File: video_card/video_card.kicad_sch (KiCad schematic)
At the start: 22 parts, among them J1 Bus, J2 DE15_Receptacle_HighDensity, J3 H_SYNC_TEST, J4 V_SYNC_TEST, J5 VSYNC_INT_EN, J6 INT_EN, U1 Upduino v3.1, U2 25.175 MHz, U3 SN74LVC4245A, U4 SN74LVC4245A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

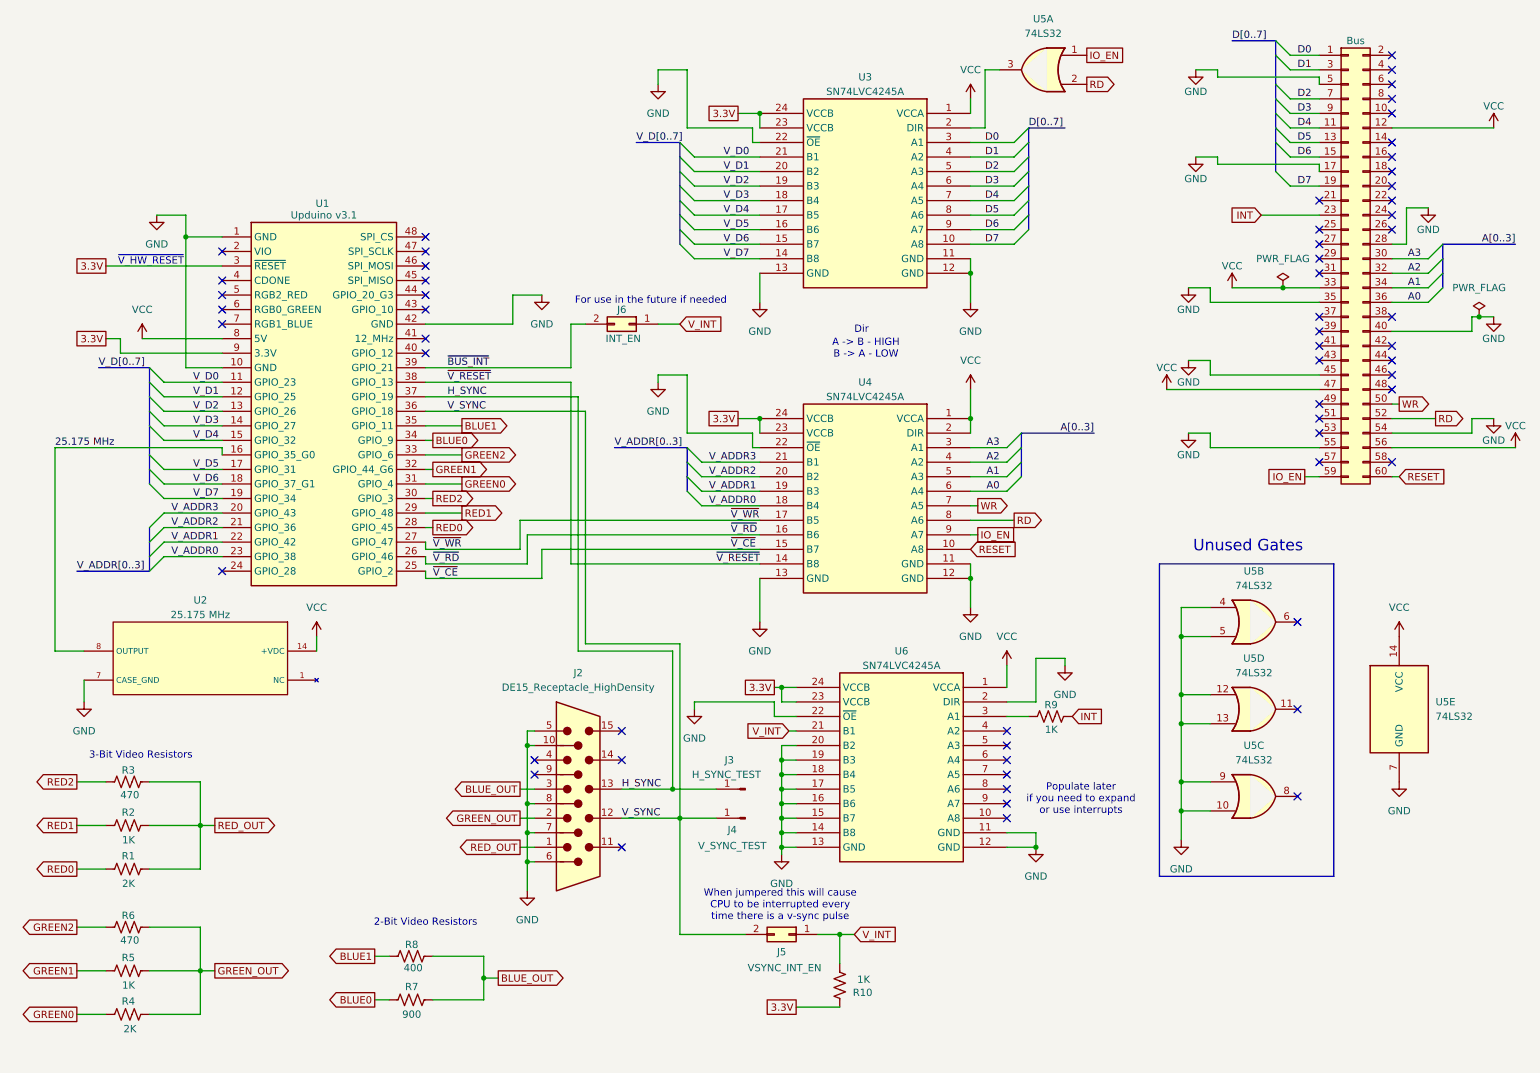
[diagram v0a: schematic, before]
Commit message: Swapped out '4245' on the INT signal to a more simple transistor circuit
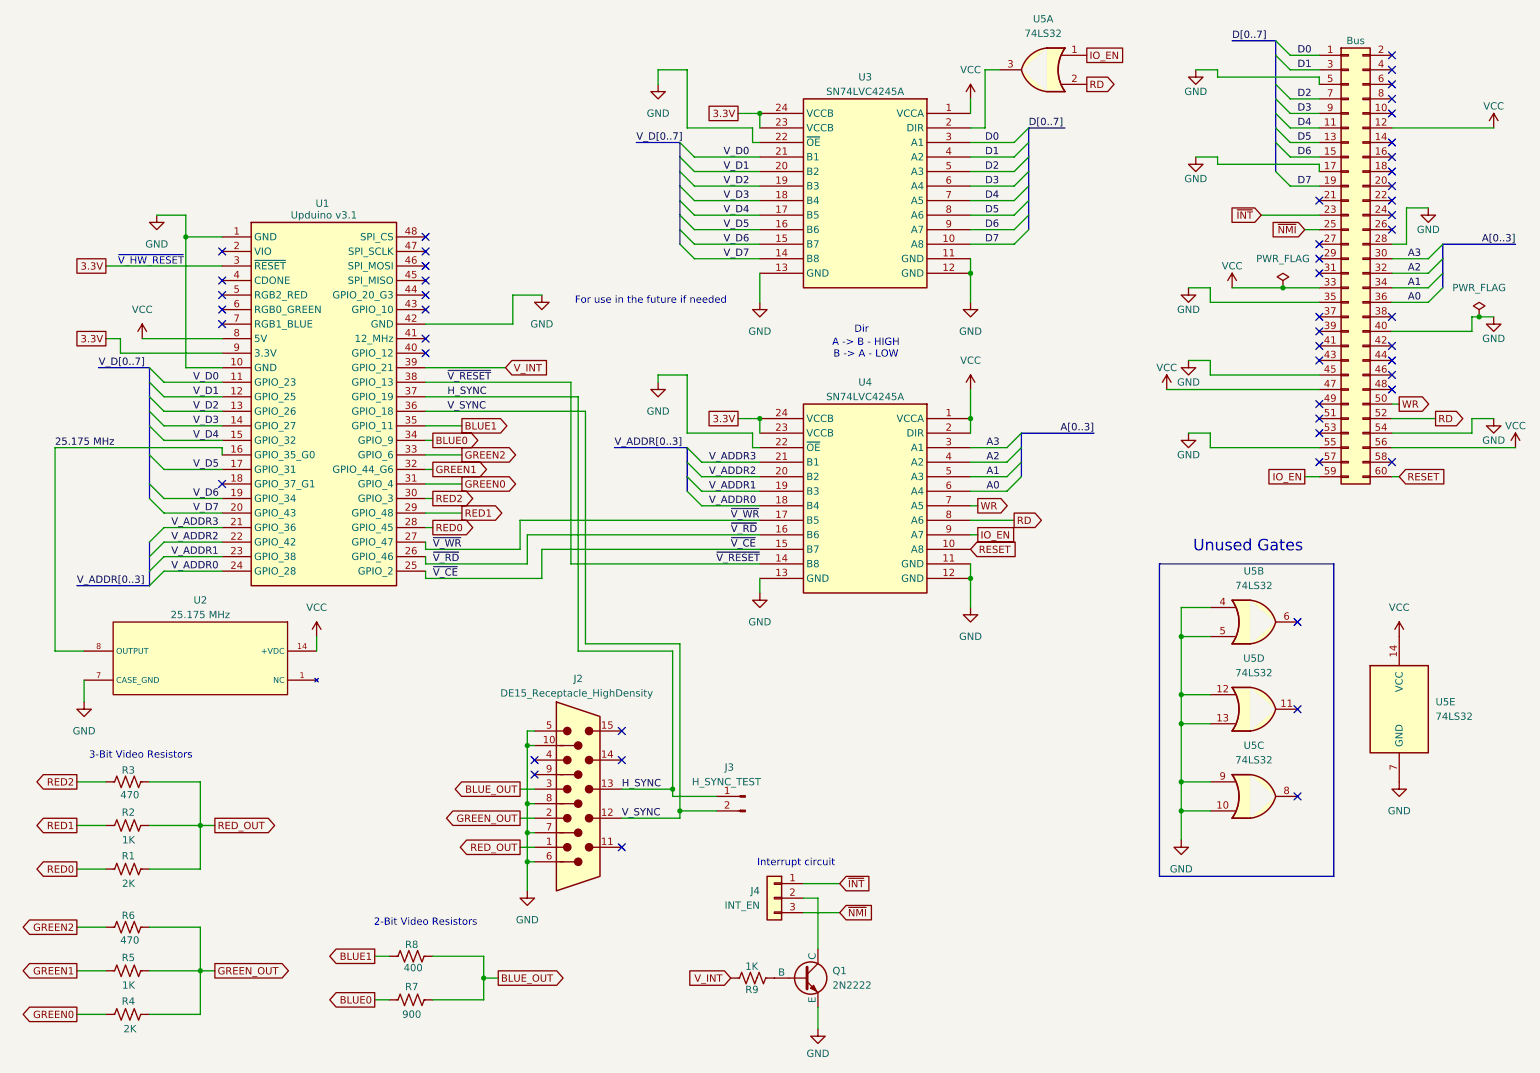
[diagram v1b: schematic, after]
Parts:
- removed J4: V_SYNC_TEST, Connector_PinHeader_2.54mm:PinHeader_1x01_P2.54mm_Vertical, symbol Connector:Conn_01x01_Pin
- removed J5: VSYNC_INT_EN, Connector_PinHeader_2.54mm:PinHeader_2x01_P2.54mm_Vertical, symbol Connector_Generic:Conn_02x01
- removed J6: INT_EN, Connector_PinHeader_2.54mm:PinHeader_2x01_P2.54mm_Vertical, symbol Connector_Generic:Conn_02x01
- removed R10: 1K, Resistor_THT:R_Axial_DIN0207_L6.3mm_D2.5mm_P10.16mm_Horizontal, symbol Device:R_US
- removed U6: SN74LVC4245A, Z80 Parts:SN74LVC4245A, symbol Z80-Parts:SN74LVC4245A
- added J4: INT_EN, Connector_PinHeader_2.54mm:PinHeader_1x03_P2.54mm_Vertical, symbol Connector_Generic:Conn_01x03
- added Q1: 2N2222, Package_TO_SOT_THT:TO-92, symbol Simulation_SPICE:NPN
- J3: footprint Connector_PinHeader_2.54mm:PinHeader_1x01_P2.54mm_Vertical -> Connector_PinHeader_2.54mm:PinHeader_1x02_P2.54mm_Vertical; symbol Connector:Conn_01x01_Pin -> Connector:Conn_01x02_Pin
- U3, U4: footprint Z80 Parts:SN74LVC4245A -> Z80 Parts:SN74LVC4245ADWR
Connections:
- net ~{BUS_INT} is gone; now on net V_INT: U1.39 (GPIO_21)
- net GND: now also Q1.3 (E)
- net V_ADDR0: now also U1.24 (GPIO_28); no longer U1.23 (GPIO_38)
- net V_ADDR1: now also U1.23 (GPIO_38); no longer U1.22 (GPIO_42)
- net V_ADDR2: now also U1.22 (GPIO_42); no longer U1.21 (GPIO_36)
- net V_ADDR3: now also U1.21 (GPIO_36); no longer U1.20 (GPIO_43)
- net V_D6: now also U1.19 (GPIO_34); no longer U1.18 (GPIO_37_G1)
- net V_D7: now also U1.20 (GPIO_43); no longer U1.19 (GPIO_34)
- net V_INT: now also R9.2
- net V_SYNC: now also J3.2 (Pin_2)
- net at R9.1: now also Q1.2 (B)
- net ~{NMI}: now reaches J1.25 (Pin_25)
- net ~{NMI}: now also J4.3 (Pin_3)
- net INT renamed ~{INT}
- net ~{INT}: now also J4.1 (Pin_1); no longer R9.2
- new net: J4.2 (Pin_2), Q1.1 (C)
- no-connect marks 60 -> 52
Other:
- note added: "Interrupt circuit"
- note removed: "Populate later if you need to expand or use interrupts"
- note removed: "When jumpered this will cause CPU to be interrupted every time there is a v-sync pulse"
